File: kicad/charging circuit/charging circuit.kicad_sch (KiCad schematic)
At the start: 7 parts, among them J1 Conn_01x04, K1 Relay_DPST-NO, K2 Relay_DPST-NO, K3 Relay_DPST-NO, SW2 SW_Push_Open

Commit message: charging circuit
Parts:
- added D1, D2: LED, symbol Device:LED
- added F1: L50QS150, symbol Device:Fuse_Small
- added HVP800_interlock: Conn_01x02, symbol Connector_Generic:Conn_01x02
- added J2: Conn_01x06, symbol Connector_Generic:Conn_01x06
- added J3: Conn_01x08, symbol Connector_Generic:Conn_01x08
- added K4: Relay_SPST-NC, symbol Relay:Relay_SPST-NC
- added R1: 3k, symbol Device:R
- added R2, R3: 15k, symbol Device:R
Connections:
- net +12V: now also D1.2 (A), D2.2 (A), J2.4 (Pin_4), J3.7 (Pin_7)
- net CANH: now also J2.2 (Pin_2), J3.3 (Pin_3)
- net CANL: now also J2.1 (Pin_1), J3.2 (Pin_2)
- net GND: now also J2.5 (Pin_5), J3.4 (Pin_4), K4.A2
- net HV+: now also K4.12, R3.2
- net HV-: now also R1.2, R2.2
- net TS+: now also F1.1; no longer K1.13
- net at IMD.1 (Pin_1): now also HVP800_interlock.1 (Pin_1); no longer SW2.2 (B)
- net ENABLE: now reaches J1.3 (Pin_3), SW2.1 (A)
- net ENABLE: now also J2.6 (Pin_6), K4.A1
- new net: D1.1 (K), J3.5 (Pin_5)
- new net: D2.1 (K), J3.6 (Pin_6)
- new net: F1.2, K1.13
- new net: K4.11, R1.1
- new net: HVP800_interlock.2 (Pin_2), SW2.2 (B)
- new net CAN_GND: J2.3 (Pin_3)
- new net CHASSIS_GND: J3.1 (Pin_1)
- new net TSMP+: R3.1
- new net TSMP-: R2.1
- no-connect marks 0 -> 1
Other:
- note added: "Shutdown circuit"

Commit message: bunch of schemes
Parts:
- AIR_H: renamed from K1; value Relay_DPST-NO -> KILOVAC EV200-HAANA
- AIR_L: renamed from K2; value Relay_DPST-NO -> KILOVAC EV200-HAANA
- F1: value L50QS150 -> L50QS150 150A
- HVP800_interlock: value Conn_01x02 -> TE_HVP800
- J1: value Conn_01x04 -> TE HVP800
- K3: value Relay_DPST-NO -> KILOVAC EV200-HAANA
- K4: value Relay_SPST-NC -> GIGAVAC PNC113BDA
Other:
- note added: "Alpha Wire Eco Wire Series 6712 0.2mm^2"
- note added: "Ningbo KBE FHL2G 25mm^2 TS"
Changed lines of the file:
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@@
 	(text "Shutdown circuit"
 		(exclude_from_sim no)
-		(at 139.192 80.518 0)
-		(effects
-			(font
-				(size 1.27 1.27)
+		(at 143.256 72.136 0)
+		(effects
+			(font
+				(size 5 5)
 			)
 		)
@@
 			(font
 				(size 12.7 12.7)
+			)
+		)
+	)
+	(text "Ningbo\nKBE FHL2G\n25mm^2\nTS"
+		(exclude_from_sim no)
+		(at 247.396 72.644 0)
+		(effects
+			(font
+				(size 5 5)
+			)
+		)
+	)
+	(text "Alpha Wire\nEco Wire Series 6712\n0.2mm^2"
+		(exclude_from_sim no)
+		(at 145.796 55.626 0)
+		(effects
+			(font
+				(size 5 5)
 			)
 		)
@@
 			)
 		)
-		(property "Value" "Relay_DPST-NO"
+		(property "Value" "KILOVAC 	EV200-HAANA"
 			(at 82.55 54.61 90)
 			(effects
@@
 		(fields_autoplaced yes)
 		(property "Reference" "F1"
-			(at 195.58 60.96 0)
-			(effects
-				(font
-					(size 1.27 1.27)
-				)
-			)
-		)
-		(property "Value" "L50QS150"
-			(at 195.58 63.5 0)
-			(effects
-				(font
-					(size 1.27 1.27)
+			(at 195.58 58.42 0)
+			(effects
+				(font
+					(size 1.27 1.27)
+				)
+			)
+		)
+		(property "Value" "L50QS150 150A"
+			(at 195.58 62.23 0)
+			(effects
+				(font
+					(size 3 3)
 				)
 			)
@@
 		(dnp no)
 		(fields_autoplaced yes)
-		(property "Reference" "K1"
+		(property "Reference" "AIR_H"
 			(at 207.01 45.72 90)
 			(effects
@@
 			)
 		)
-		(property "Value" "Relay_DPST-NO"
+		(property "Value" "KILOVAC 	EV200-HAANA"
 			(at 207.01 48.26 90)
 			(effects
@@
 			(project ""
 				(path "/3be6bc6a-149a-4182-aeea-983f7e00c2a9"
-					(reference "K1")
+					(reference "AIR_H")
 					(unit 1)
 				)
@@
 			)
 		)
-		(property "Value" "Relay_SPST-NC"
+		(property "Value" "GIGAVAC	PNC113BDA"
 			(at 114.3 101.6 90)
 			(effects
@@
 		(dnp no)
 		(fields_autoplaced yes)
-		(property "Reference" "K2"
+		(property "Reference" "AIR_L"
 			(at 207.01 88.9 90)
 			(effects
@@
 			)
 		)
-		(property "Value" "Relay_DPST-NO"
+		(property "Value" "KILOVAC 	EV200-HAANA"
 			(at 207.01 91.44 90)
 			(effects
@@
 			(project "charging circuit"
 				(path "/3be6bc6a-149a-4182-aeea-983f7e00c2a9"
-					(reference "K2")
+					(reference "AIR_L")
 					(unit 1)
 				)
@@
 		(on_board yes)
 		(dnp no)
-		(fields_autoplaced yes)
 		(property "Reference" "HVP800_interlock"
 			(at 124.46 86.3599 90)
 			(effects
 				(font
-					(size 1.27 1.27)
-				)
-				(justify left)
-			)
-		)
-		(property "Value" "Conn_01x02"
-			(at 124.46 88.8999 90)
+					(size 3 3)
+				)
+				(justify left)
+			)
+		)
+		(property "Value" "TE_HVP800"
+			(at 124.46 90.1699 90)
 			(effects
 				(font
@@
 		(fields_autoplaced yes)
 		(property "Reference" "J1"
-			(at 83.82 101.6 0)
-			(effects
-				(font
-					(size 1.27 1.27)
-				)
-			)
-		)
-		(property "Value" "Conn_01x04"
-			(at 83.82 104.14 0)
-			(effects
-				(font
-					(size 1.27 1.27)
-				)
-			)
+			(at 83.82 99.06 0)
+			(effects
+				(font
+					(size 1.27 1.27)
+				)
+			)
+		)
+		(property "Value" "TE HVP800"
+			(at 83.82 102.87 0)
+			(effects
+				(font
+					(size 3 3)
+				)
+			)

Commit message: charging can
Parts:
- added J10, J17: Amphenol PL00Y-301-10M8, symbol Connector_Generic:Conn_01x01
- added J12, J16: Amphenol PL00X-301-10M8, symbol Connector_Generic:Conn_01x01
- D1: value LED -> AMS
- D2: value LED -> TSAL_G
- F1: value L50QS150 150A -> A50QS200
- J1: value TE HVP800 -> amphenol pl00x and pl00y
- pl00xinterlock: renamed from HVP800_interlock; value TE_HVP800 -> amphenolpl00x
- renumbered K3 to OBCrelay, K4 to Precharge
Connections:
- net HV-: now also J10.1 (Pin_1), J17.1 (Pin_1)
- net TS+: now also J12.1 (Pin_1), J16.1 (Pin_1)
- net ENABLE_OBC: now reaches AIR_H.A2, AIR_L.A2, BMS.2 (Pin_2), OBCrelay.A2
- net ENABLE_OBC: now also J2.6 (Pin_6), Precharge.A1
- net ENABLE: no longer names the net of J1.3 (Pin_3), SW2.1 (A)
- net ENABLE: no longer J2.6 (Pin_6), Precharge.A1
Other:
- note added: "Enables the Obc"
- note added: "PL28X-301-50"
- note added: "PL28Y-301-50"
- moved on the sheet: D1, D2, J2, J3, R2, R3

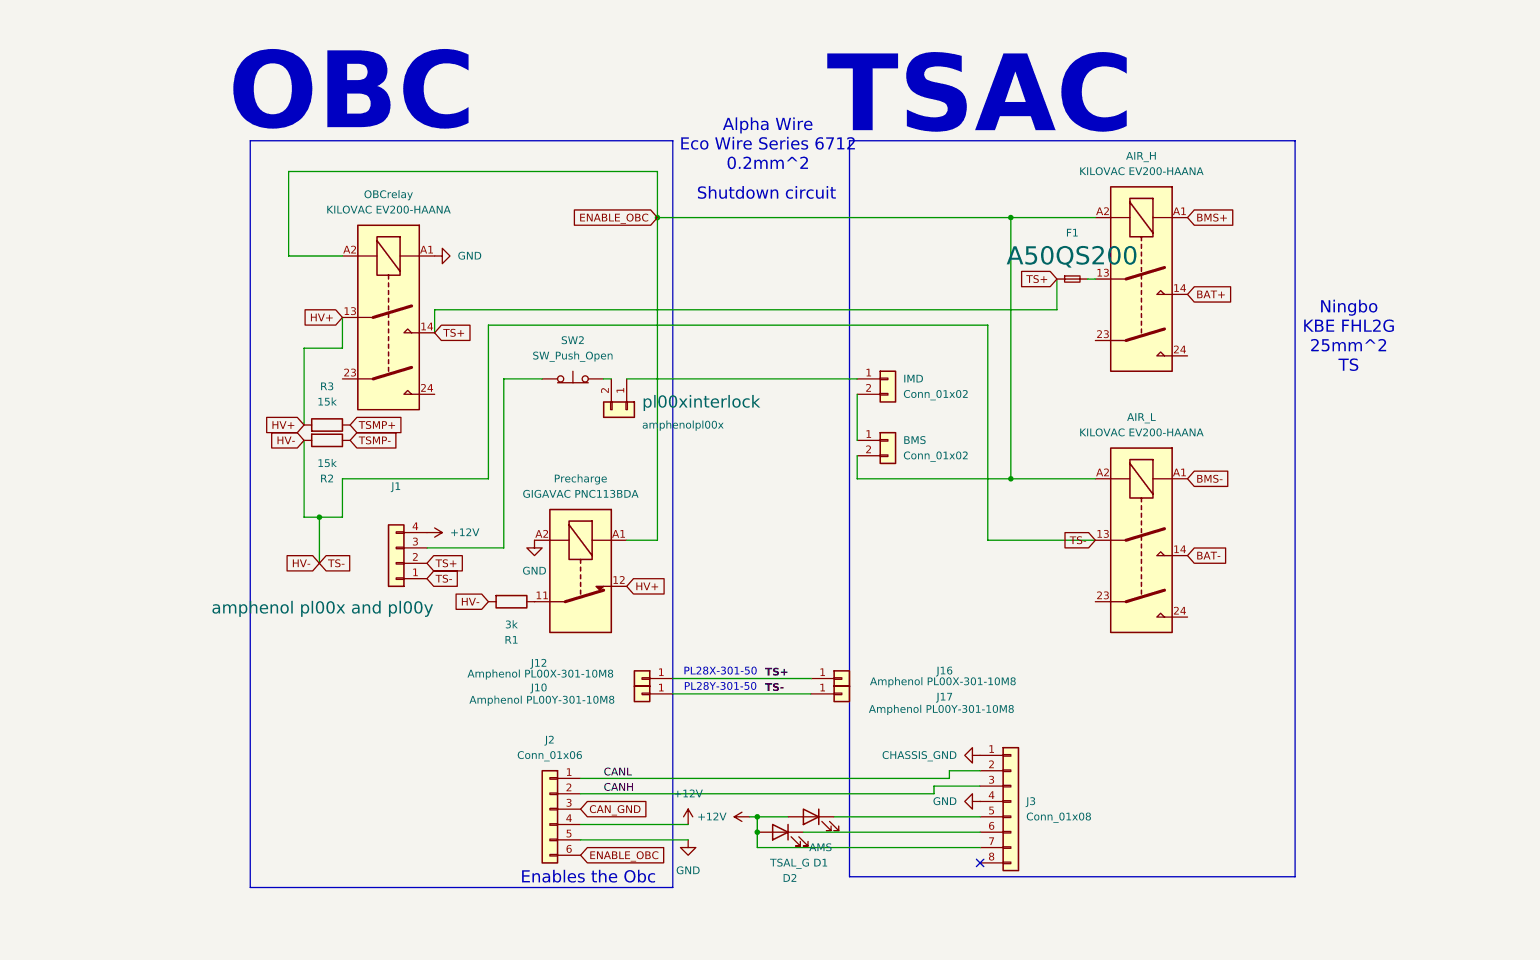
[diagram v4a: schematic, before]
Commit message: Update charging circuit and TS schematics connections
Removed obsolete backup files and updated global labels in TS schematics. Modified the charging circuit schematic to use a 3-pin connector instead of 4-pin, adjusted wire routing, connector placements, and updated component values and labels for improved clarity and accuracy.
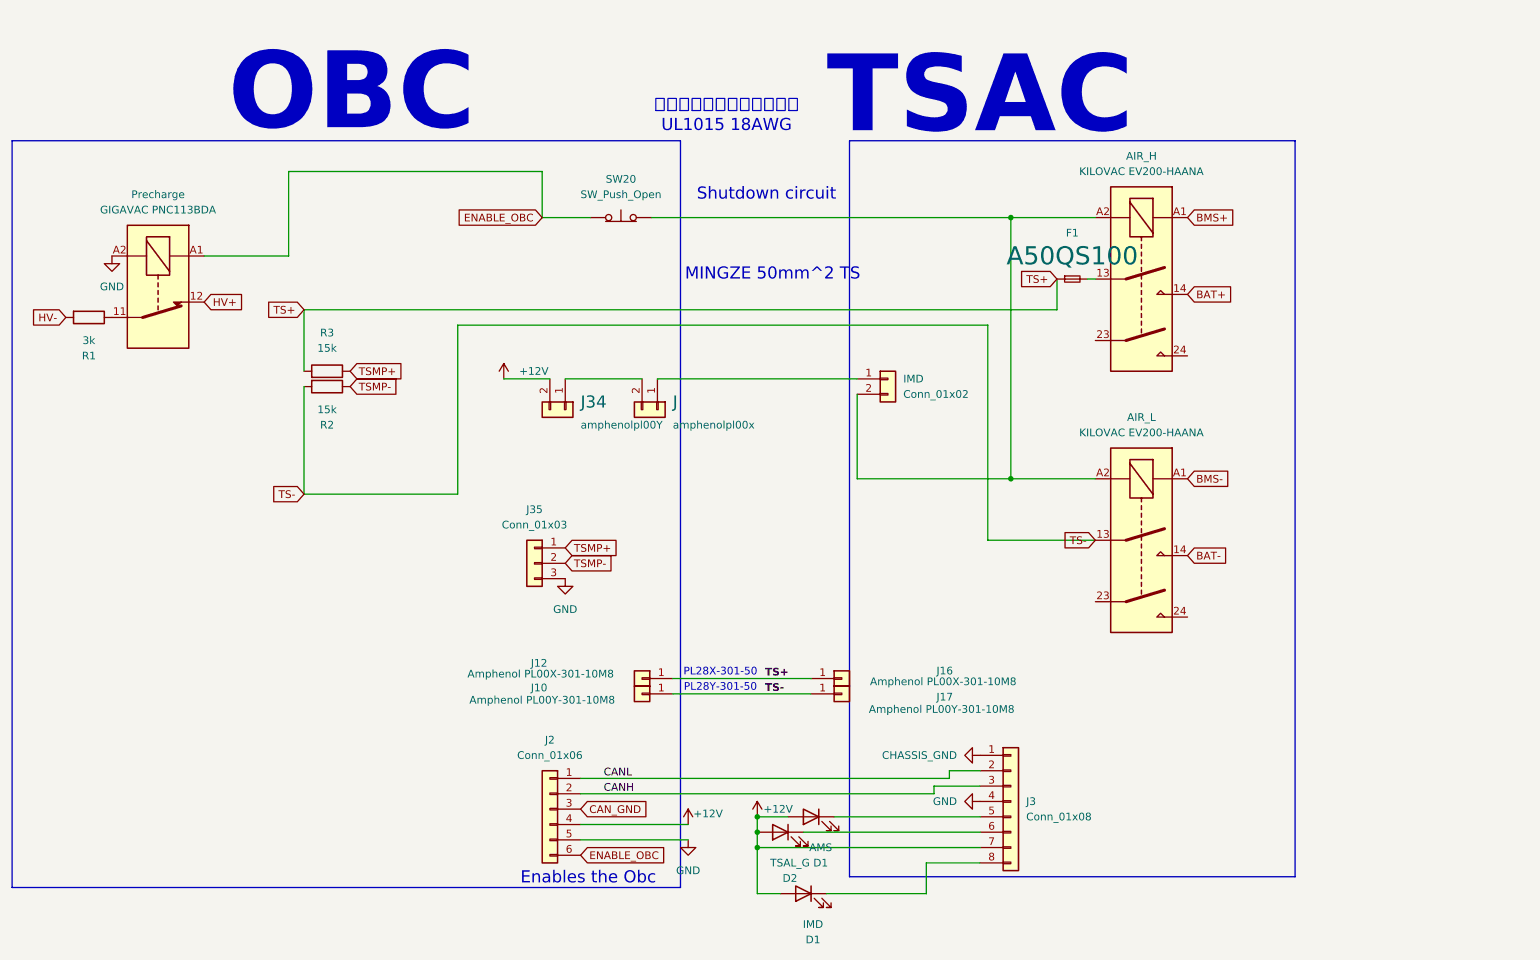
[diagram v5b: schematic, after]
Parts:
- removed BMS: Conn_01x02, symbol Connector_Generic:Conn_01x02
- removed J1: amphenol pl00x and pl00y, symbol Connector_Generic:Conn_01x04
- removed OBCrelay: KILOVAC EV200-HAANA, symbol Relay:Relay_DPST-NO
- added D1: IMD, symbol Device:LED
- added J34: amphenolpl00Y, symbol Connector_Generic:Conn_01x02
- added J35: Conn_01x03, symbol Connector_Generic:Conn_01x03
- F1: value A50QS200 -> A50QS100
- renumbered pl00xinterlock to J, SW2 to SW20
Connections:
- net +12V: now also D1.2 (A), J34.2 (Pin_2)
- net ENABLE_OBC: now also SW20.1 (A); no longer AIR_H.A2, AIR_L.A2
- net GND: now also J35.3 (Pin_3)
- net HV+: no longer R3.2
- net HV-: no longer AIR_L.13, J10.1 (Pin_1), J17.1 (Pin_1), R2.2
- net TS+: now also R3.2
- net TSMP+: now also J35.1 (Pin_1)
- net TSMP-: now also J35.2 (Pin_2)
- net at IMD.2 (Pin_2): now also AIR_H.A2, AIR_L.A2, SW20.2 (B)
- net at J3.8 (Pin_8): now also D1.1 (K)
- net at J.2 (Pin_2): now also J34.1 (Pin_1); no longer SW20.2 (B)
- new net TS-: AIR_L.13, J10.1 (Pin_1), J17.1 (Pin_1), R2.2
- no-connect marks 1 -> 0
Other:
- note added: "MINGZE 50mm^2 TS"
- note added: "上海佳玉机电设备有限公司 UL1015 18AWG"
- note removed: "Alpha Wire Eco Wire Series 6712 0.2mm^2"
- note removed: "Ningbo KBE FHL2G 25mm^2 TS"
- moved on the sheet: J, Precharge, R1, R2, R3, SW20
